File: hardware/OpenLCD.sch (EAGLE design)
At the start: 41 parts, among them Q1 PNP-500mA, Q2 PNP-500mA, Q3 PNP-500mA, U1 ATMEGA328P_TQFP, U2 4BIT-RGB, U3 ADJ, U4 MCP4725, Y2 8MHZ

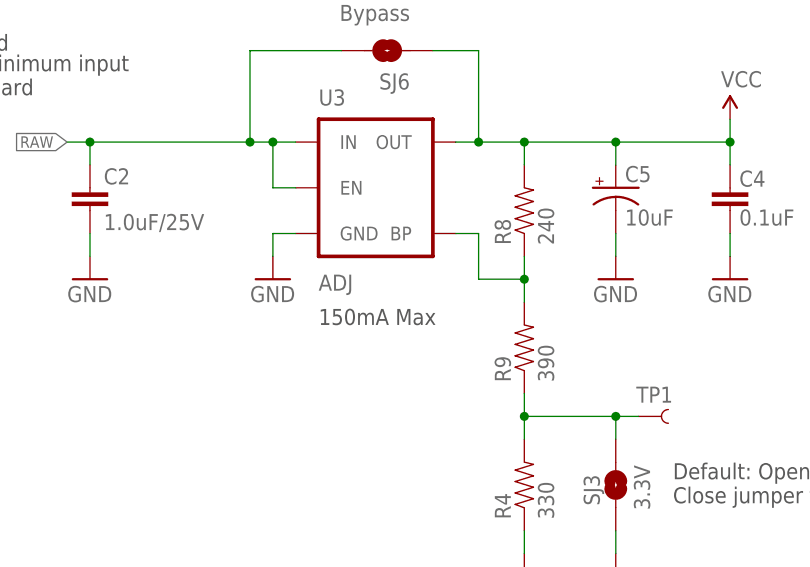
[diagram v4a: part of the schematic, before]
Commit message: Fixes for issue #4.
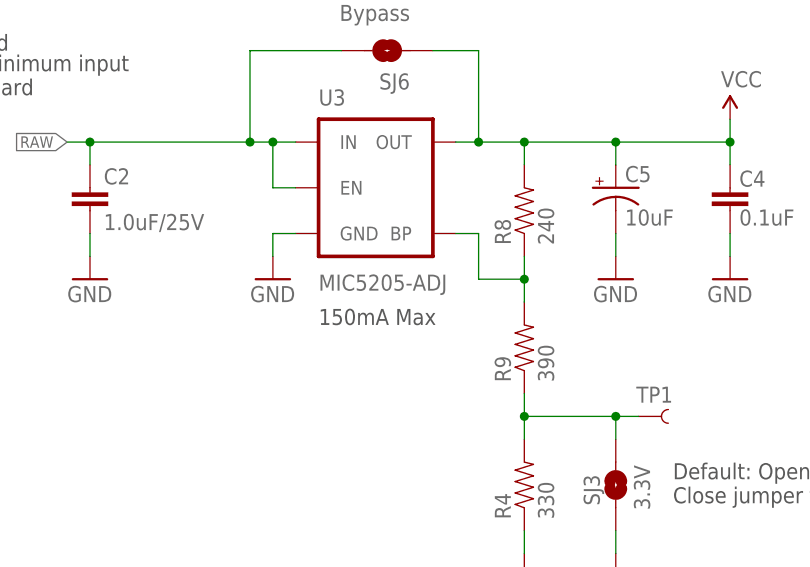
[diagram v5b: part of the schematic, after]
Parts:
- U3: value ADJ -> MIC5205-ADJ
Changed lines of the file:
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@@
 <part name="GND5" library="SparkFun" deviceset="GND" device=""/>
 <part name="SJ5" library="SparkFun-Passives" deviceset="JUMPER-PAD-2-NO" device="YES_SILK" value="Size"/>
-<part name="U3" library="SparkFun-PowerIC" deviceset="V_REG_MIC5205" device="ADJ" value="ADJ"/>
+<part name="U3" library="SparkFun-PowerIC" deviceset="V_REG_MIC5205" device="ADJ" value="MIC5205-ADJ"/>
 <part name="R4" library="SparkFun-Resistors" deviceset="330OHM1/10W1%(0603)" device="" value="330"/>
 <part name="R8" library="SparkFun-Resistors" deviceset="240OHM1/10W1%(0603)" device="" value="240"/>

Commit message: Changes the pins to work with v2 protos. Added custom char support.
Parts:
- removed C2: 1.0uF/25V, SparkFun-Capacitors:1.0UF-25V-+80/-20(0805)"
- removed C5: 10uF, SparkFun-Capacitors:10UF-16V-10%(TANT)
- removed JP3: 3-PIN SMD, SparkFun-Connectors:M03JST-SMD
- removed JP6: RESET, SparkFun-Connectors:M01PTH
- removed Q2, Q3: PNP-500mA, SparkFun-DiscreteSemi:TRANSISTOR-PNP-DDTB142TC
- removed R4: 330, SparkFun-Resistors:330OHM1/10W1%(0603)
- removed R6, R7, R8: 240, SparkFun-Resistors:240OHM1/10W1%(0603)
- removed R9: 390, SparkFun-Resistors:390OHM1/10W1%(0603)
- removed SJ1, SJ2: JUMPER-PAD-3-2OF3_NC_BY_PASTE, SparkFun-Passives:JUMPER-PAD-3-2OF3_NC_BY_PASTE
- removed SJ3: 3.3V, SparkFun-Passives:JUMPER-PAD-2-NOYES_SILK
- removed SJ6: Bypass, SparkFun-Passives:JUMPER-PAD-2-NOYES_SILK
- removed TP1: TEST-POINT3X4, SparkFun-Passives:TEST-POINT3X4
- removed U3: MIC5205-ADJ, SparkFun-PowerIC:V_REG_MIC5205ADJ
- added J1: JST, SparkFun-Connectors:CONN_03JST-PTH
- added J2: PTH, SparkFun-Connectors:CONN_03
- added J3: 3.5mm Screw Terminal, SparkFun-Connectors:CONN_03SCREW_LOCK
- added J4: Reset, SparkFun-Connectors:CONN_01PTH_NO_SILK_YES_STOP
- C1, C3: device SparkFun-Capacitors:0.1UF-25V(+80/-20%)(0603) -> SparkFun-Capacitors:0.1UF-0603-25V-(+80/-20%)
- C4: value 0.1uF -> 10uF; device SparkFun-Capacitors:0.1UF-25V(+80/-20%)(0603) -> SparkFun-Capacitors:10UF-0805-10V-10%
- JP2: device SparkFun-Connectors:M10SILK_FEMALE_PTH -> SparkFun-Connectors:CONN_10"
- R1, R3: value 10K -> 10k; device SparkFun-Resistors:10KOHM-1/10W-1%(0603)0603 -> SparkFun-Resistors:10KOHM-0603-1/10W-1%
- R10, R11: value 4.7K -> 4.7k; device SparkFun-Resistors:4.7KOHM-1/10W-1%(0603) -> SparkFun-Resistors:4.7KOHM-0603-1/10W-1%
- R5: device SparkFun-Resistors:240OHM1/10W1%(0603) -> SparkFun-Resistors:240OHM-0603-1/10W-1%
- U2: value 4BIT-RGB -> 4BIT-LCD
- Y2: value 8MHZ -> 16MHZ
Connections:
- net BL-R/W renamed BL-CONTROL
- removed net 3V-JUMPER: R4.2, R9.1, SJ3.2, TP1.1, U1.ADC6
- removed net A-BLUE: R7.1, U2.BLU
- removed net A-GREEN: R6.1, U2.GRN
- removed net BACKLIGHT1: SJ2.2, U2.A/K
- removed net BACKLIGHT2: SJ1.2, U2.K/RED
- removed net BL-B: Q3.B, U1.PB1(OC1A)
- removed net BL-G: Q2.B, U1.PD6(AIN0)
- removed net MONO/RED: R5.1, SJ1.1, SJ2.3
- removed net N$4: Q2.C, R6.2
- removed net N$5: Q3.C, R7.2
- removed net N$6: R8.1, R9.2, U3.BP
- removed net RAW: C2.1, JP2.9, JP3.1, SJ6.2, U3.EN, U3.IN
- new net BACKLIGHT: R5.1, U2.A/K
- new net SW-SCL: U1.PB1(OC1A), U4.SCL
- new net SW-SDA: U1.PB0(ICP), U4.SDA
- net GND: now also C4.2, J1.2, J2.2, J3.2, U2.K/RED; no longer C2.2, C4.1, C5.-, JP3.2, R4.1, SJ1.3, SJ2.1, SJ3.1, U3.GND
- net RST: now also J4.1; no longer JP6.1
- net RXI: now also J1.3, J2.1, J3.1; no longer JP3.3
- net SCL: no longer U4.SCL
- net SDA: no longer U4.SDA
- net VCC: now also C4.1, J1.1, J2.3, J3.3, JP2.9; no longer C4.2, C5.+, Q2.E, Q3.E, R8.2, SJ6.1, U3.OUT
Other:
- note added: "Backlight"
- note removed: "150mA Max"
- note removed: "5 to 12V Input"
- note removed: "Backlights"
- note removed: "By default the jumpers support standard single backlight. Move both jumpers to 'RGB' to work with RGB backlights."
- note removed: "Close the bypass jumper and provide board with regulated supply (5V or 3.3V) when the LCD backlight uses more than 150mA."
- note removed: "Default: Open for 5V Close jumper for 3.3V"
- note removed: "Do not change the OpenLCD I2C address to 0x60 as this will conflict with the onboard DAC."
- note removed: "In general 5V to 12V is allowed"
- note removed: "It is recommended that the minimum input voltage is 0.15V more than board operating voltage."
- note removed: "On RBG-backlit LCDs Backlight1 is Red cathode and Backlight2 is Red anode."
- note removed: "On mono-backlit LCDs Backlight1 is anode and Backlight2 is cathode."
- note removed: "Power"
- note removed: "TBD:"
- note removed: "check what is displayed above 127"
- note removed: "close 3,3v jumper by default?"
- moved on the sheet: C4, R10, R11, R3, R5, SJ4, SJ5, TP2, U2, U4
